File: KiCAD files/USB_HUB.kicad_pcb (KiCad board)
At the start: 2 copper layers, 66.5 x 89.2 mm, 23 parts, among them U1 SL2.1S

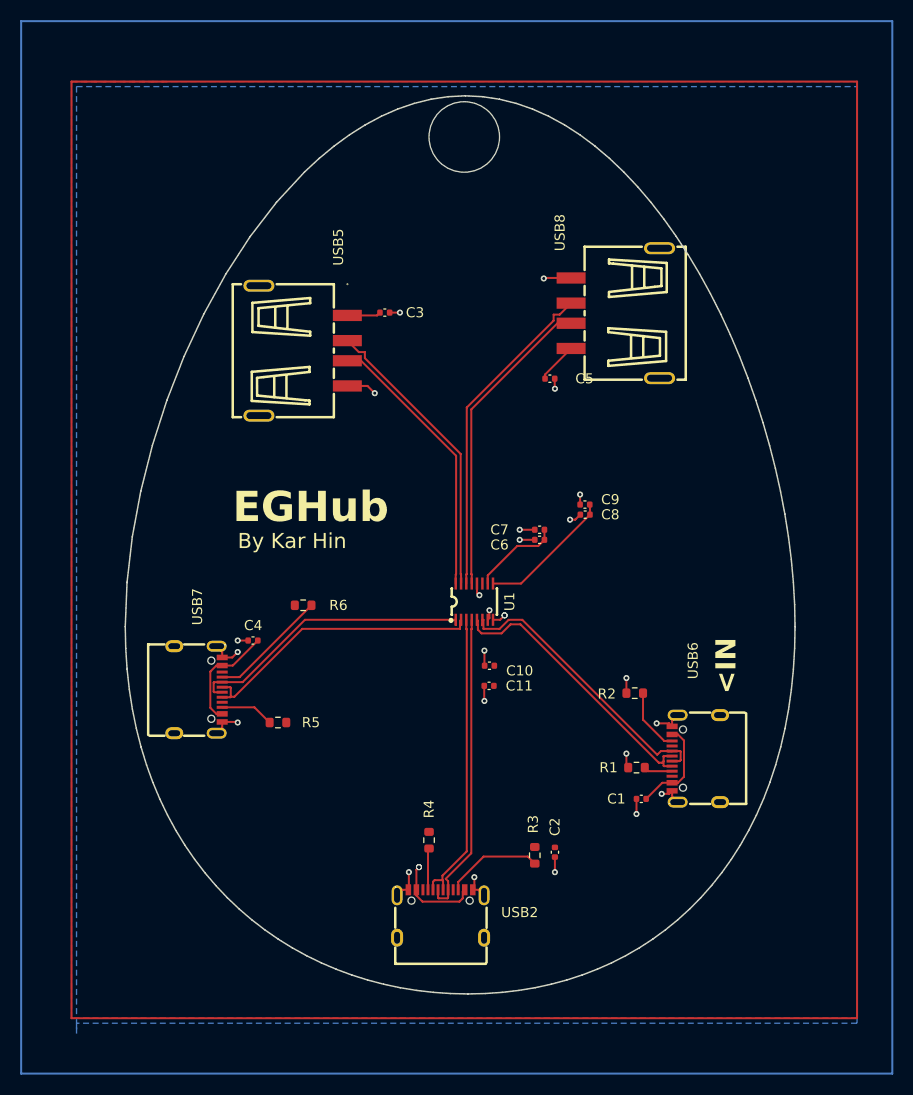
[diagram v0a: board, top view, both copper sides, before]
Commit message: Updated board design to include ESD. Not changed: Zine, README except BOM
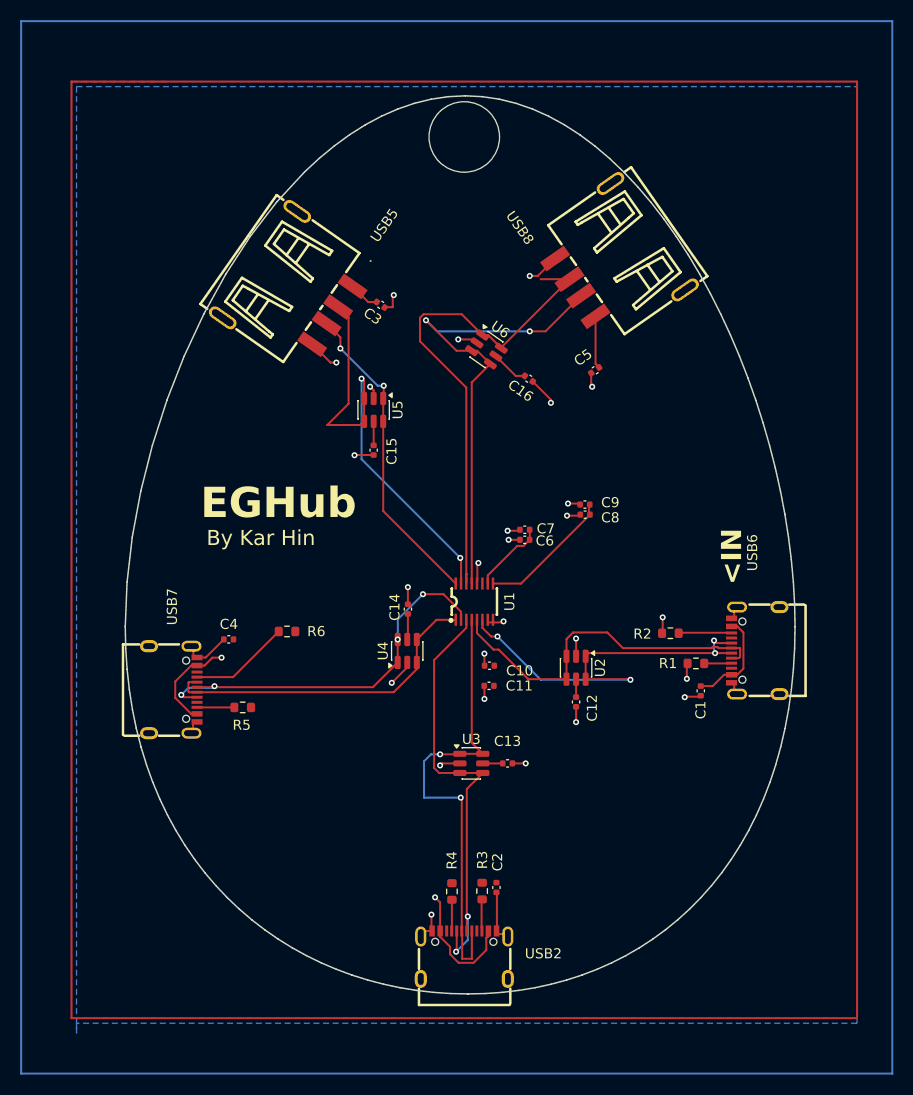
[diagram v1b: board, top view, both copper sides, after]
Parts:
- added C12: 0.1uF, Capacitor_SMD:C_0402_1005Metric, F.Cu at (156.6, 119.6)
- added C13: 0.1uF, Capacitor_SMD:C_0402_1005Metric, F.Cu at (149.8, 125.7)
- added C14: 0.1uF, Capacitor_SMD:C_0402_1005Metric, F.Cu at (139.9, 110.4)
- added C15: 0.1uF, Capacitor_SMD:C_0402_1005Metric, F.Cu at (136.5, 94.6)
- added C16: 0.1uF, Capacitor_SMD:C_0402_1005Metric, F.Cu at (151.9, 87.5)
- added U2: USBLC6-2SC6, Package_TO_SOT_SMD:SOT-23-6, F.Cu at (156.6, 116.2)
- added U3: USBLC6-2SC6, Package_TO_SOT_SMD:SOT-23-6, F.Cu at (146.2, 125.7)
- added U4: USBLC6-2SC6, Package_TO_SOT_SMD:SOT-23-6, F.Cu at (139.8, 114.5)
- added U5: USBLC6-2SC6, Package_TO_SOT_SMD:SOT-23-6, F.Cu at (136.5, 90.6)
- added U6: USBLC6-2SC6, Package_TO_SOT_SMD:SOT-23-6, F.Cu at (147.7, 84.6)
- moved C1 12.2 mm to (169.0, 118.5), turned to -90 degrees
- moved USB6 12.2 mm to (174.4, 114.5)
- moved R1 11.9 mm to (168.5, 115.8)
- moved R2 6.92 mm to (166.0, 112.8)
- moved C2 6.78 mm to (148.7, 138.0)
- moved R3 6.32 mm to (147.3, 138.4)
- moved USB5 6.07 mm to (128.8, 78.7), turned to -125 degrees
- moved R4 5.58 mm to (144.3, 138.4)
- moved USB8 5.09 mm to (160.1, 75.9), turned to 125 degrees
- moved USB2 4.72 mm to (145.5, 144.7)
- moved C5 4.57 mm to (158.5, 86.7), turned to -145 degrees
- moved R5 3.81 mm to (123.5, 120.1)
- moved R6 3.05 mm to (127.9, 112.6), turned to 180 degrees
- moved USB7 2.50 mm to (116.6, 118.4)
- moved C4 2.41 mm to (122.1, 113.4)
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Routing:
- net /DP4: track 32.5 -> 50.5 mm
- net /DN4: track 30.8 -> 48.2 mm, vias 0 -> 2
- net /DN3: track 29.1 -> 46.1 mm, vias 0 -> 2
- net +5V: track 37.0 -> 54.0 mm
- net GND: track 43.2 -> 27.2 mm, vias 25 -> 26
- net /DN1: track 29.7 -> 43.6 mm, vias 0 -> 2
- net /DP: track 29.5 -> 42.1 mm, vias 0 -> 4
- net /DP2: track 29.7 -> 39.5 mm, vias 0 -> 4
- net /DP1: track 30.6 -> 40.4 mm, vias 0 -> 2
- net Net-(USB2-CC2): track 9.71 -> 0.00 mm
- net /DN: track 29.5 -> 36.1 mm
- net Net-(USB6-CC2): track 6.40 -> 0.00 mm
- net Net-(USB7-CC2): track 5.34 -> 0.00 mm
- net Net-(USB2-CC1): track 4.14 -> 0.00 mm
- net /DP3: track 27.4 -> 31.5 mm, vias 0 -> 2
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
